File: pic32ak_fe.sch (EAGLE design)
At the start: 86 parts, among them IC1 NCP1117LPST33T3G, IC2 SFH6916, J1 CONBNC001, J2 CONBNC001, J3 CONBNC001, J4 CONBNC001, J5 5227222-3, SW1 PTS635SL50LFS, SW2 PTS635SL50LFS, U1 PIC32AK1216GC41064-E/PT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

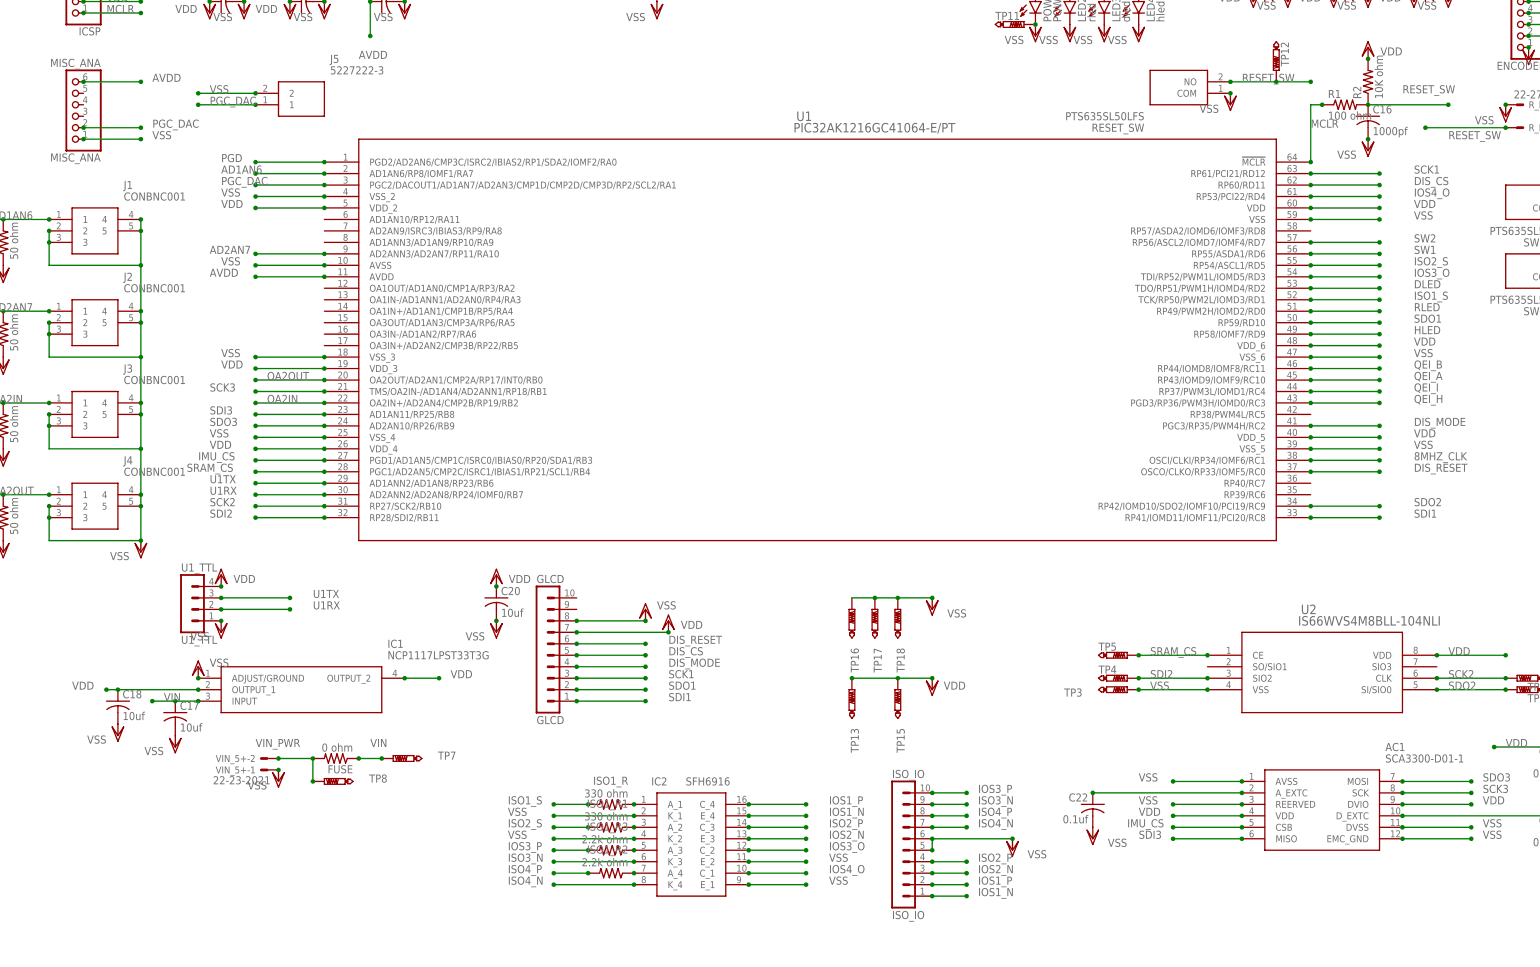
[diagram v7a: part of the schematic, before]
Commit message: all pins conneced on PCB
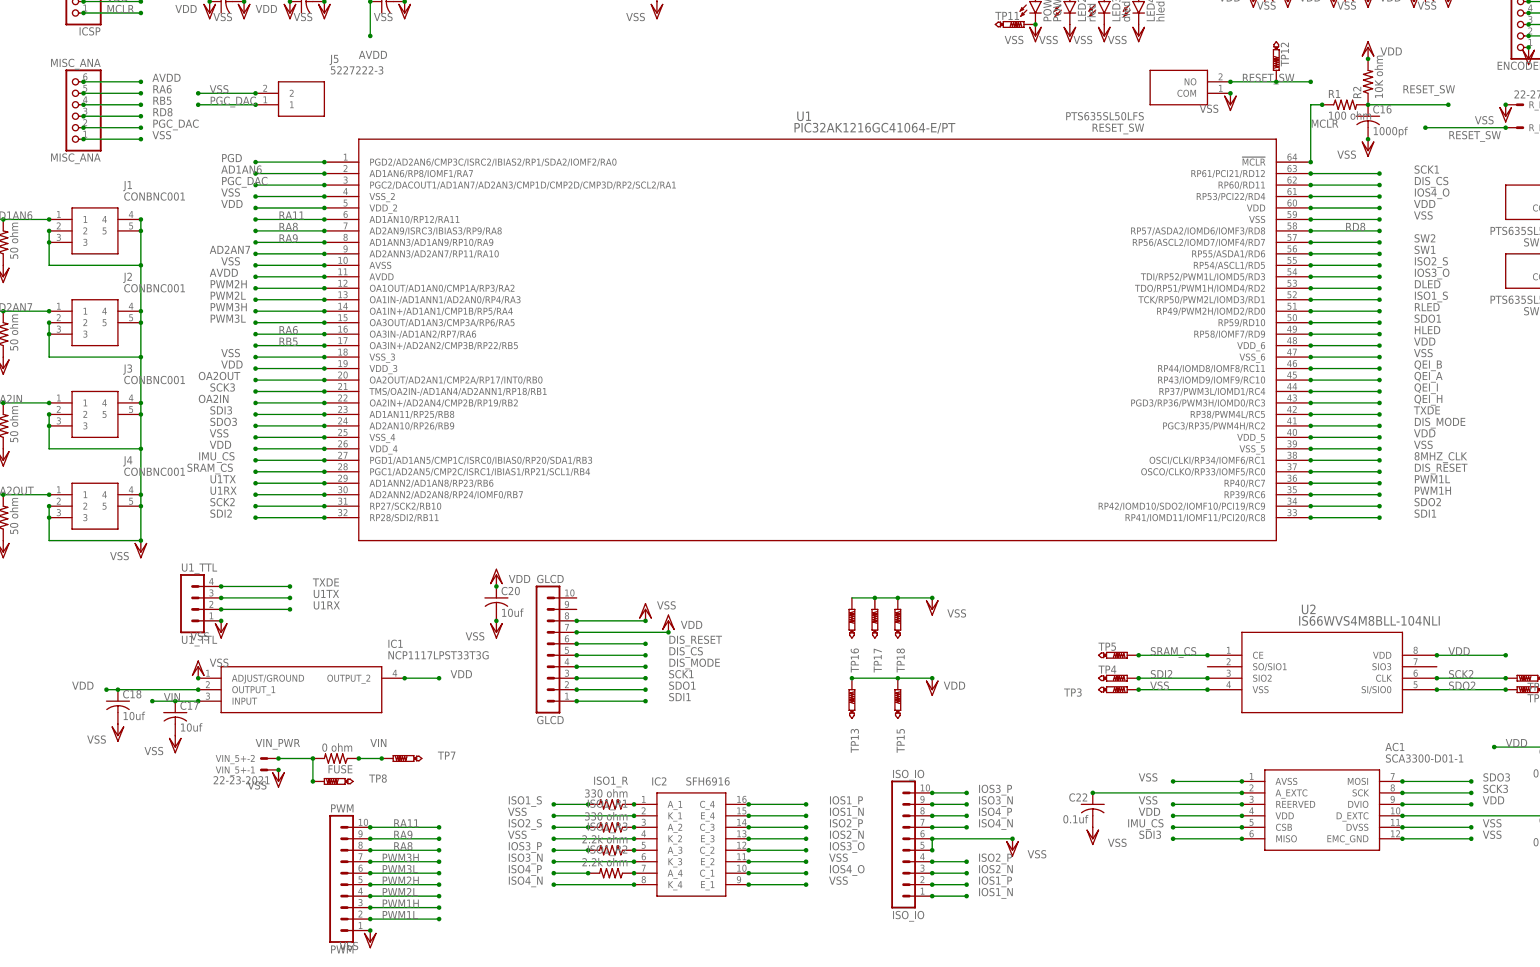
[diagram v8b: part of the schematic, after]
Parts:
- added PWM: PWM, con-lstb:MA10-1
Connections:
- new net PWM1H: PWM.3, U1.RP39/RC6
- new net PWM1L: PWM.2, U1.RP40/RC7
- new net PWM2H: PWM.5, U1.OA1OUT/AD1AN0/CMP1A/RP3/RA2
- new net PWM2L: PWM.4, U1.OA1IN-/AD1ANN1/AD2AN0/RP4/RA3
- new net PWM3H: PWM.7, U1.OA1IN+/AD1AN1/CMP1B/RP5/RA4
- new net PWM3L: PWM.6, U1.OA3OUT/AD1AN3/CMP3A/RP6/RA5
- new net RA11: PWM.10, U1.AD1AN10/RP12/RA11
- new net RA6: MISC_ANA.5, U1.OA3IN-/AD1AN2/RP7/RA6
- new net RA8: PWM.8, U1.AD2AN9/ISRC3/IBIAS3/RP9/RA8
- new net RA9: PWM.9, U1.AD1ANN3/AD1AN9/RP10/RA9
- new net RB5: MISC_ANA.4, U1.OA3IN+/AD2AN2/CMP3B/RP22/RB5
- new net RD8: MISC_ANA.3, U1.RP57/ASDA2/IOMD6/IOMF3/RD8
- new net TXDE: U1.RP38/PWM4L/RC5, U1_TTL.4
- net VDD: no longer U1_TTL.4
- net VSS: now also PWM.1
